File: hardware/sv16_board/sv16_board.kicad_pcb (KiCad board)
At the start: 4 copper layers, 100 x 100 mm, 132 parts, among them J1 JTAG, J10 CONSOLE, J2 JTAG-1.27, J3 EXP-A, J4 EXP-B, J5 EXP-C, J6 MOTOR, J7 SPARE (not fitted), J8 USB-C, J9 7-12 V, Q1 2N7002, Q2 BC817, Q3 AO3401, Q4 BC807, SW1 RESET, SW2 RECONFIG, U1 LFE5U-12F-6TG144C, U2 W25Q64JVSSIQ, U3 W25Q64JVSSIQ, U4 CH340C, U5 LM2596S-3.3, U6 MP1584EN, U7 AMS1117-2.5, U8 USBLC6-2SC6, Y1 25 MHz XO

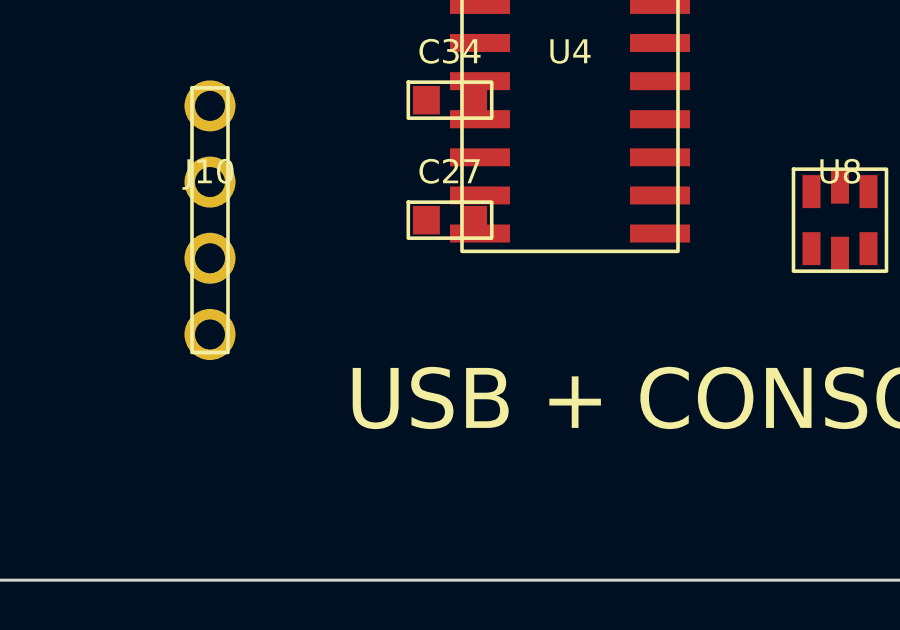
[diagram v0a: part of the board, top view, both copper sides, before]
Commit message: CH340G needs a 12 MHz crystal; the HC49/US part is a passive crystal
Second pass over the cart with the parts the user just named.

* FPGA confirmed unchanged: LFE5U-12F-6TG144C, so the pin map, the LPF and the
  bitstream flow are untouched.

* U4 is a CH340G, not the CH340C the design assumes. The G version has no
  internal clock: it needs a 12 MHz crystal between XI (pin 7) and XO (pin 8)
  plus two 22 pF load capacitors. Added as Y2, C36, C37 with the datasheet pin
  numbers in PCB_COMPONENTS.md section 4.4 (1 GND, 2 TXD, 3 RXD, 4 V3, 5 UD+,
  6 UD-, 7 XI, 8 XO, 13 DTR#, 15 R232, 16 VCC), the crystal wiring in BOARD.md
  section 7.4 sheet 4, and the three new footprints in the board file. Pin 13 is
  still DTR# so the auto-reconfigure path is unchanged; the G's modem pins are
  left open. A CH340C remains a pin-compatible drop-in that needs none of it.

* Y1: the user's "25 MHz HC49/US crystal oscillator" is a 2-pin PASSIVE crystal.
  The ECP5 has no on-chip crystal driver, so it cannot drive clk_25m - the board
  would configure and then have no clock, no console and no boot. Recorded as
  OQ-B14 and as correction 5 in PCB_COMPONENTS.md section 10, with both ways
  out: buy an active 3.3 V 4-pin XO (~Rs 110, footprint already in the board
  file), or build a Pierce oscillator around the crystal with a 74LVC1G04, 1 M
  feedback resistor and 2 x 22 pF. The board file keeps the active-XO footprint
  and the component is now labelled "ACTIVE XO (4-pin)" so it is hard to miss.

* hardware/cart/RECONCILED.md gains a second-batch section covering all three
  parts, and FOOTPRINT_RECONCILE.md gains rows for the CH340G pinout, Y2 and the
  Y1 pin-count check.

Verified: board file regenerates with 135 footprints, 582 pads, 459 on nets over
131 nets, self-check OK; make lint passes; BOARD.pdf and PCB_COMPONENTS.pdf
re-rendered.

Co-authored-by: arena-agent <297053741+arena-agent@users.noreply.github.com>
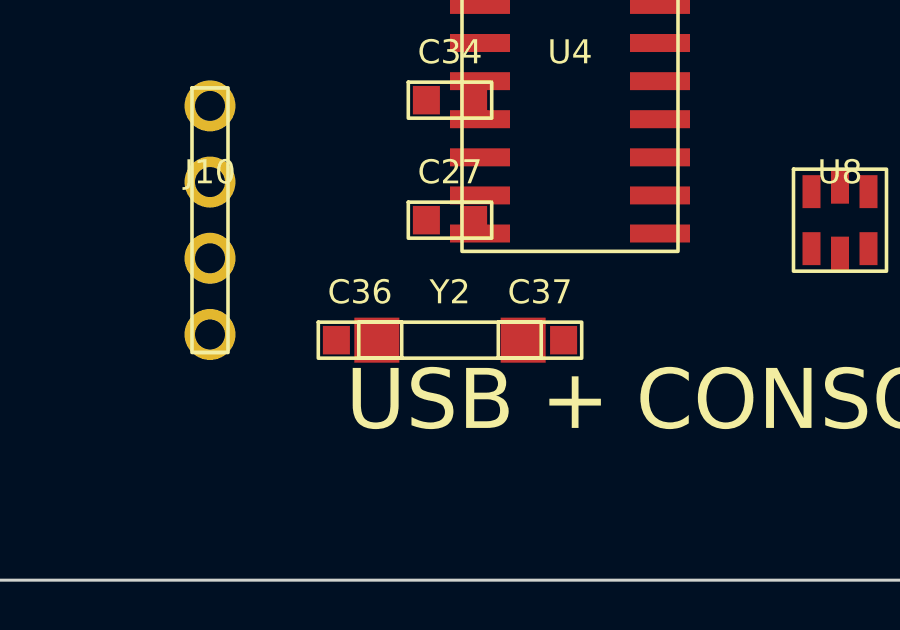
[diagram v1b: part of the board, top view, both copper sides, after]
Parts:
- added C36: C36, Capacitor_SMD:C_0603_1608Metric, F.Cu at (67.0, 92.0)
- added C37: C37, Capacitor_SMD:C_0603_1608Metric, F.Cu at (73.0, 92.0)
- added Y2: 12 MHz + 22 pF (CH340G), Crystal:Crystal_HC49-4H_Vertical, F.Cu at (70.0, 92.0)
- Y1: value 25 MHz XO -> 25 MHz ACTIVE XO (4-pin)
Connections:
- U4 pad 7: (no net) -> Y2_XI
- U4 pad 8: (no net) -> Y2_XO

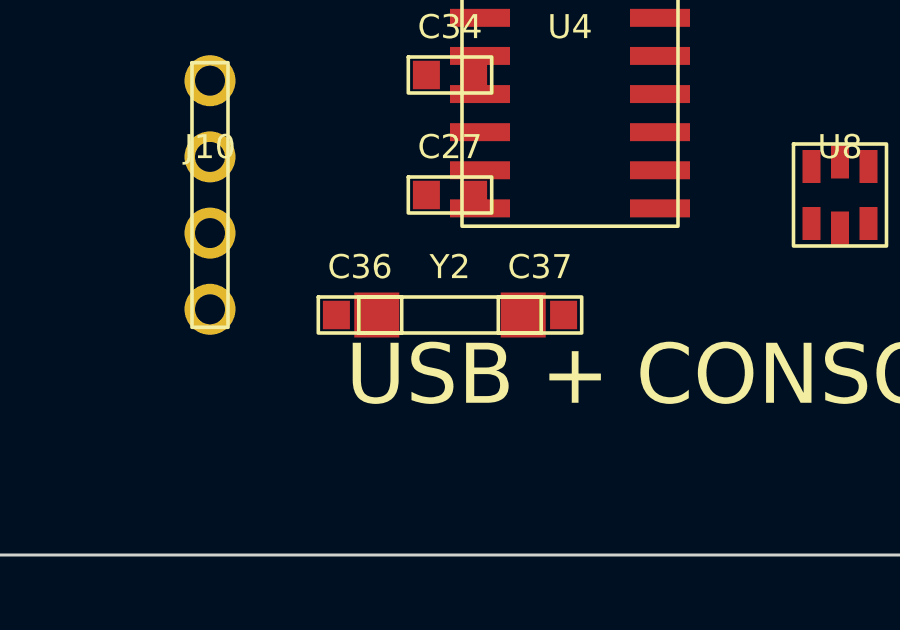
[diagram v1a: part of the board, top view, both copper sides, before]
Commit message: Answer the "12 MHz passive crystal" question in the docs
The CH340G is the one place on this board where a passive two-pin crystal is
exactly right - it has its own inverter on XI/XO, unlike the ECP5, which has no
crystal driver at all. Three details were missing from the docs, so they are in
now:

* Y2 must be 12 MHz and nothing else: the datasheet's FCLK window is
  11.98-12.02 MHz, so the 25 MHz part cannot be substituted here either.
* C36/C37 must match the crystal's load capacitance: 22 pF for a CL = 12 pF
  crystal, 33 pF for the common CL = 20 pF HC49/US type. WCH quotes both values
  in different datasheet revisions, which is why the rule is now written down
  instead of one number.
* An active 12 MHz oscillator may drive XI with XO left open, per the datasheet
  ("When using an external oscillator feed the clock signal into XI pin, and
  leave XO pin unconnected") - recorded as the alternative to Y2/C36/C37.

Y2's footprint in the board file is now a real HC49/US through-hole part
(4.88 mm lead spacing, 1.5 mm pads, 0.8 mm drill) matching KiCad's
Crystal:Crystal_HC49-4H_Vertical pad for pad, rather than an SMD stand-in.

Verified: board regenerates (135 footprints, 582 pads, 459 on nets, 131 nets,
self-check OK), make lint passes, both PDFs re-rendered.

Co-authored-by: arena-agent <297053741+arena-agent@users.noreply.github.com>
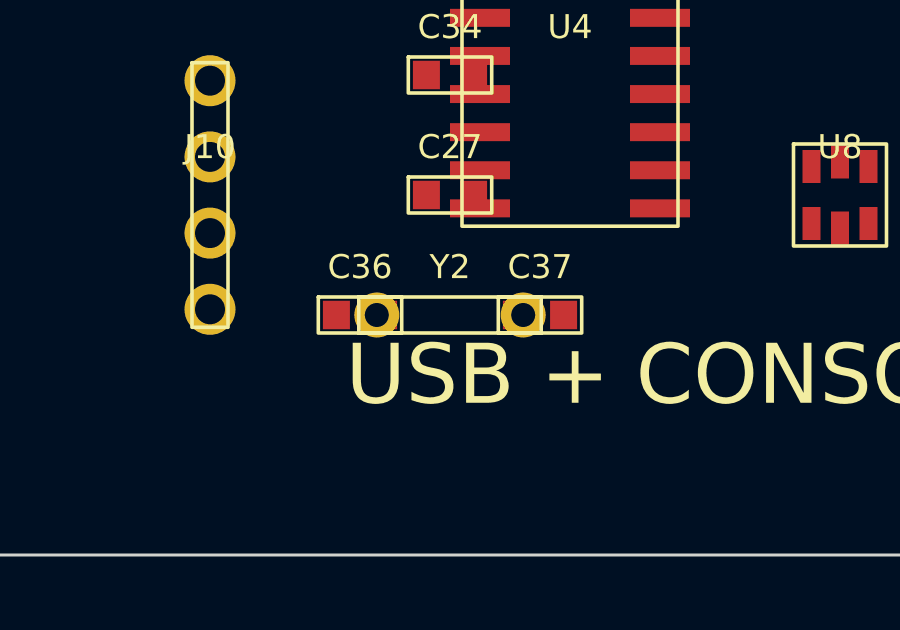
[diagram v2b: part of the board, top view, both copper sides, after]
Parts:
- Y2: value 12 MHz + 22 pF (CH340G) -> 12 MHz (CH340G clock)
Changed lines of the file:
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@@
     (pad "4" smd rect (at 1.000 0.800) (size 1.200 1.000) (layers "F.Cu" "F.Paste" "F.Mask") (net 4 "3V3"))
   )
-  (footprint "Crystal:Crystal_HC49-4H_Vertical" (layer "F.Cu") (at 70.00 92.00 0) (attr smd)
+  (footprint "Crystal:Crystal_HC49-4H_Vertical" (layer "F.Cu") (at 70.00 92.00 0) (attr through_hole)
     (fp_text reference "Y2" (at 0 -1.6) (layer "F.SilkS") (effects (font (size 0.8 0.8) (thickness 0.15))))
-    (fp_text value "12 MHz + 22 pF (CH340G)" (at 0 1.6) (layer "F.Fab") (effects (font (size 0.8 0.8) (thickness 0.15))))
+    (fp_text value "12 MHz (CH340G clock)" (at 0 1.6) (layer "F.Fab") (effects (font (size 0.8 0.8) (thickness 0.15))))
     (fp_rect (start -3.04 -0.60) (end 3.04 0.60) (layer "F.SilkS") (stroke (width 0.12) (type solid)) (fill none))
     (fp_rect (start -3.04 -0.60) (end 3.04 0.60) (layer "F.Fab") (stroke (width 0.10) (type solid)) (fill none))
-    (pad "1" smd rect (at -2.440 0.000) (size 1.500 1.500) (layers "F.Cu" "F.Paste" "F.Mask") (net 59 "Y2_XI"))
-    (pad "2" smd rect (at 2.440 0.000) (size 1.500 1.500) (layers "F.Cu" "F.Paste" "F.Mask") (net 60 "Y2_XO"))
+    (pad "1" thru_hole circle (at -2.440 0.000) (size 1.500 1.500) (drill 0.800) (layers "*.Cu" "*.Mask") (net 59 "Y2_XI"))
+    (pad "2" thru_hole circle (at 2.440 0.000) (size 1.500 1.500) (drill 0.800) (layers "*.Cu" "*.Mask") (net 60 "Y2_XO"))
   )
   (footprint "Package_TO_SOT_SMD:SOT-23" (layer "F.Cu") (at 10.00 70.00 0) (attr smd)

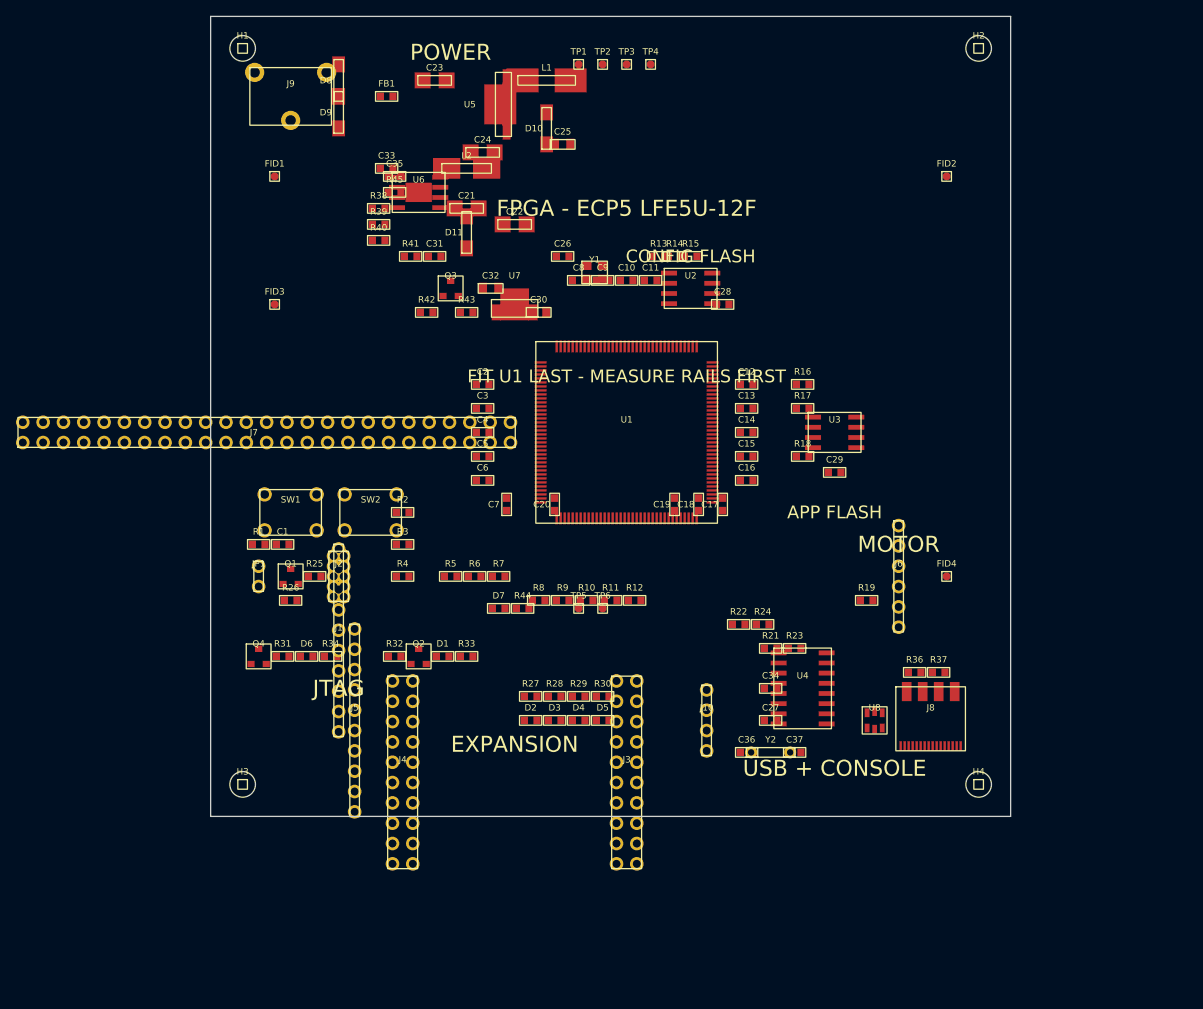
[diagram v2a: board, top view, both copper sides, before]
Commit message: Rebuild the KiCad board onto the parts actually bought
The board file no longer describes a design nobody ordered. Every part in the
cart is now in it, with the pinouts and support parts those parts require.

Power tree (was the LM2596S-3.3 / AMS1117-2.5 fallback, which is not what the
cart contains):

* U5 is the AP62300TWU-7, TSOT-26, pins 1 GND / 2 SW / 3 VIN / 4 FB / 5 EN /
  6 BST. Synchronous, so D10 is deleted. Added C38 100 nF bootstrap, R46/R47
  feedback (33 k / 10 k against the T variant's 0.763 V = 3.28 V) and R48/R49
  on EN - which matters, because EN's absolute maximum is 6 V and must never be
  tied to the 12 V input.

* U7 is the LP5907MFX-2.5, SOT-23-5 (1 IN, 2 GND, 3 EN, 4 NC, 5 OUT), fed from
  3V3. Its EN pin replaces the whole P-FET load switch: Q3, R42 and the 4.7 uF
  gate capacitor are gone, and R43 100 k / C32 470 nF now give the 2V5 rail its
  ~21 ms delay. C42 10 uF was added because the part is only stable into a
  low-ESR ceramic output capacitor.

* Packages from the cart: R38 0402; R9-R12/R31/R33/R34/R39/R46/R47/R49 1206;
  R2-R4/R27-R30/R36/R37 0805; C21 the D-case tantalum; C22 6.3x5.4; C23/C24
  8x10.5; L1/L2 the CD54 10 uH parts. U4's value string now says CH340G.

* Four SS34s are bought, three are fitted (D8/D9 input ORing, D11 the MP1584
  catch diode); the fourth is a spare.

Board-as-a-project, not just a file:

* sv16_board.kicad_pro - net classes with the widths from PCB_COMPONENTS.md
  section 7, so the router starts with the right rules.
* Two GND zones defined: a solid plane on In1.Cu and a pour on B.Cu. Outlines
  only; KiCad fills them on the first Fill All Zones (B).
* The generator now also rejects duplicate net declarations, not just duplicate
  references.

Board regenerates clean: 141 footprints, 596 pads, 472 on nets, 133 nets, two
zones, self-check OK on stock python. PCB_COMPONENTS.md gained the AP62300 and
LP5907 pin tables, the package map and corrections 6-7 (the AP62300/LP5907
support parts still to buy, an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
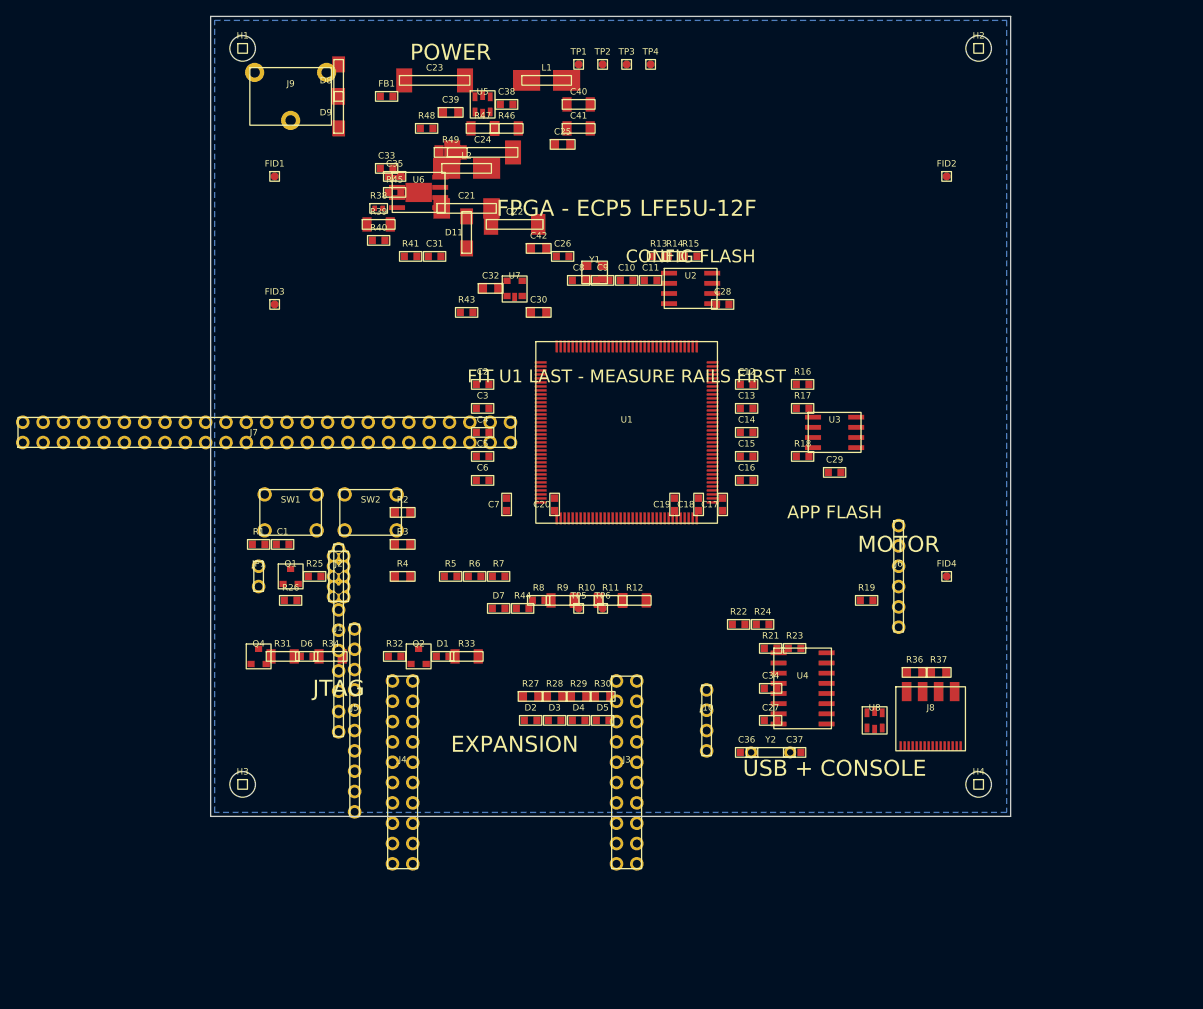
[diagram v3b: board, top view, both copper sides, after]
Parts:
- removed D10: SS34, Diode_SMD:D_SMA
- removed Q3: AO3401, Package_TO_SOT_SMD:SOT-23
- removed R42: R42, Resistor_SMD:R_0603_1608Metric
- added C38: 100nF, Capacitor_SMD:C_0603_1608Metric, F.Cu at (37.0, 11.0)
- added C39: 10uF, Capacitor_SMD:C_0805_2012Metric, F.Cu at (30.0, 12.0)
- added C40: 22uF, Capacitor_SMD:C_1206_3216Metric, F.Cu at (46.0, 11.0)
- added C41: 22uF, Capacitor_SMD:C_1206_3216Metric, F.Cu at (46.0, 14.0)
- added C42: 10uF, Capacitor_SMD:C_0805_2012Metric, F.Cu at (41.0, 29.0)
- added R46: 33k, Resistor_SMD:R_1206_3216Metric, F.Cu at (37.0, 14.0)
- added R47: 10k, Resistor_SMD:R_1206_3216Metric, F.Cu at (34.0, 14.0)
- added R48: 100k, Resistor_SMD:R_0603_1608Metric, F.Cu at (27.0, 14.0)
- added R49: 33k, Resistor_SMD:R_1206_3216Metric, F.Cu at (30.0, 17.0)
- C1: value C1 -> 100nF
- C10: value C10 -> 100nF
- C11: value C11 -> 100nF
- C12: value C12 -> 100nF
- C13: value C13 -> 100nF
- C14: value C14 -> 100nF
- C15: value C15 -> 100nF
- C16: value C16 -> 100nF
- C17: value C17 -> 100nF
- C18: value C18 -> 100nF
- C19: value C19 -> 100nF
- C2: value C2 -> 100nF
- C20: value C20 -> 100nF
- C21: value C21 -> 100uF 25V tant; footprint Capacitor_SMD:CP_Elec_6.3x5.4 -> Capacitor_Tantalum_SMD:CP_EIA-7343-31_Kemet-D
- C22: value C22 -> 22uF 63V; footprint Capacitor_SMD:CP_Elec_5x5.4 -> Capacitor_SMD:CP_Elec_6.3x5.4
- C23: value C23 -> 470uF 25V; footprint Capacitor_SMD:CP_Elec_10x10.2 -> Capacitor_SMD:CP_Elec_8x10.5
- C24: value C24 -> 220uF 16V; footprint Capacitor_SMD:CP_Elec_8x6.9 -> Capacitor_SMD:CP_Elec_8x10.5
- C25: value C25 -> 10uF
- C26: value C26 -> 100nF
- C27: value C27 -> 100nF
- C28: value C28 -> 100nF
- C29: value C29 -> 100nF
- C3: value C3 -> 100nF
- C30: value C30 -> 10uF
- C31: value C31 -> 470nF
- C32: value C32 -> 470nF
- C33: value C33 -> 100nF
- C34: value C34 -> 100nF
- C35: value C35 -> 100nF
- C36: value C36 -> 100nF
- C37: value C37 -> 100nF
- C4: value C4 -> 100nF
- C5: value C5 -> 100nF
- C6: value C6 -> 100nF
- C7: value C7 -> 100nF
- C8: value C8 -> 100nF
- C9: value C9 -> 100nF
- L1: value 33 uH -> 10 uH; footprint Inductor_SMD:L_Bourns_SRR1260 -> Inductor_SMD:L_Sunlord_SWPA6045S
- R10, R11, R12, R31, R33, R34, R9: footprint Resistor_SMD:R_0603_1608Metric -> Resistor_SMD:R_1206_3216Metric
- R2, R27, R28, R29, R3, R30, R4: footprint Resistor_SMD:R_0603_1608Metric -> Resistor_SMD:R_0805_2012Metric
- R36: value R36 -> 5.1k; footprint Resistor_SMD:R_0603_1608Metric -> Resistor_SMD:R_0805_2012Metric
- R37: value R37 -> 5.1k; footprint Resistor_SMD:R_0603_1608Metric -> Resistor_SMD:R_0805_2012Metric
- R38: value R38 -> 12.4k; footprint Resistor_SMD:R_0603_1608Metric -> Resistor_SMD:R_0402_1005Metric
- R39: value R39 -> 33k; footprint Resistor_SMD:R_0603_1608Metric -> Resistor_SMD:R_1206_3216Metric
- R40: value R40 -> 100k
- R41: value R41 -> 100k
- R43: value R43 -> 100k
- R45: value R45 -> 10k
- U4: value CH340C -> CH340G
- U5: value LM2596S-3.3 -> AP62300TWU-7; footprint Package_TO_SOT_SMD:TO-263-5_TabPin3 -> Package_TO_SOT_SMD:SOT-23-6
- U7: value AMS1117-2.5 -> LP5907MFX-2.5; footprint Package_TO_SOT_SMD:SOT-223-3_TabPin2 -> Package_TO_SOT_SMD:SOT-23-5
- turned U5 to 0 degrees
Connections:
- net U5_OUT renamed U5_SW
- C30 pad 1: U7_VIN -> 3V3
- C32 pad 1: Q3_G -> U7_EN
- C32 pad 2: VM_IN -> GND
- R43 pad 1: Q3_G -> 3V3
- R43 pad 2: VM_IN -> U7_EN
- U5 pad 1: VM_IN -> GND
- U5 pad 3: GND -> VM_IN
- U5 pad 4: 3V3 -> U5_FB
- U5 pad 5: GND -> U5_EN
- U7 pad 1: GND -> 3V3
- U7 pad 2: 2V5 -> GND
- U7 pad 3: U7_VIN -> U7_EN
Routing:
- added copper zone on B.Cu, net GND
- added copper zone on In1.Cu, net GND
